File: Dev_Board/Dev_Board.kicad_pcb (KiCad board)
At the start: 2 copper layers, 13 parts

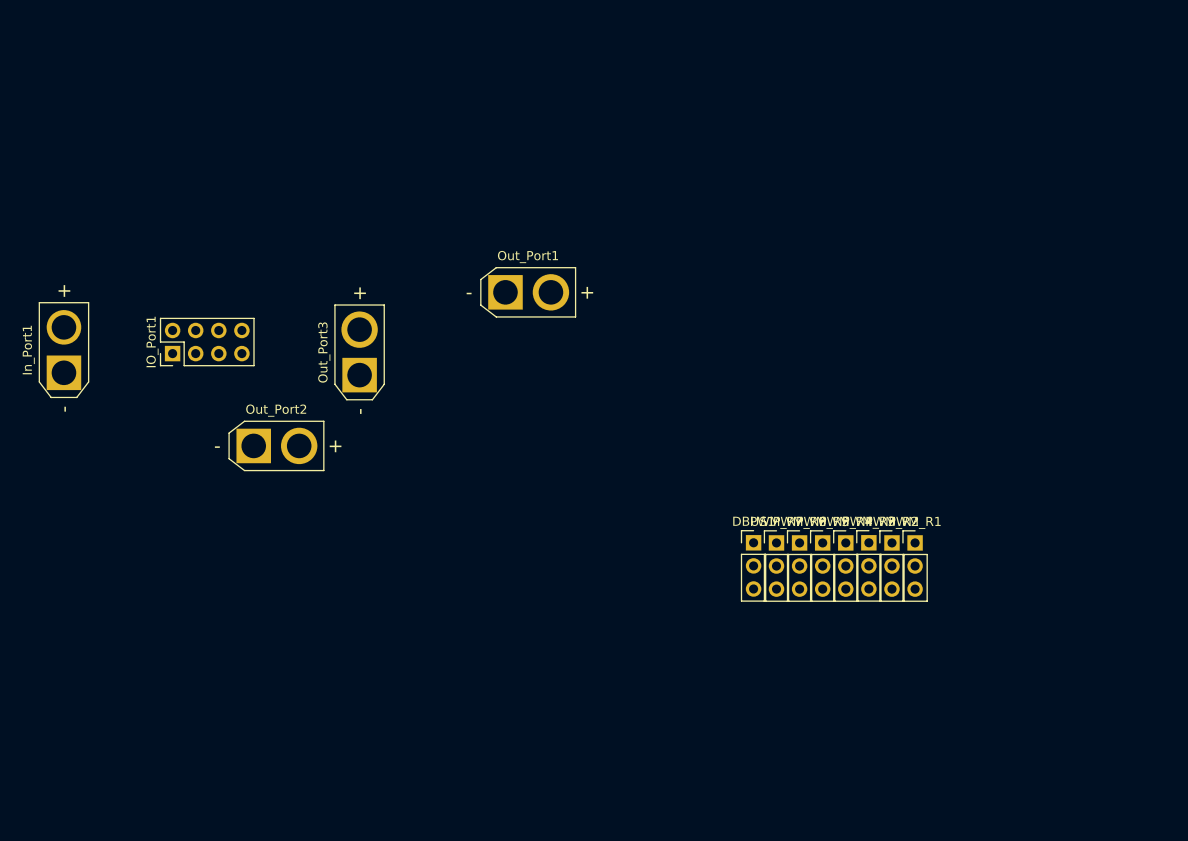
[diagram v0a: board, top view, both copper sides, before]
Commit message: added more pins to have different sets on the front and back sides. also changed the courtyards on some footprints because of errors. there are still like 3 courtyard errors
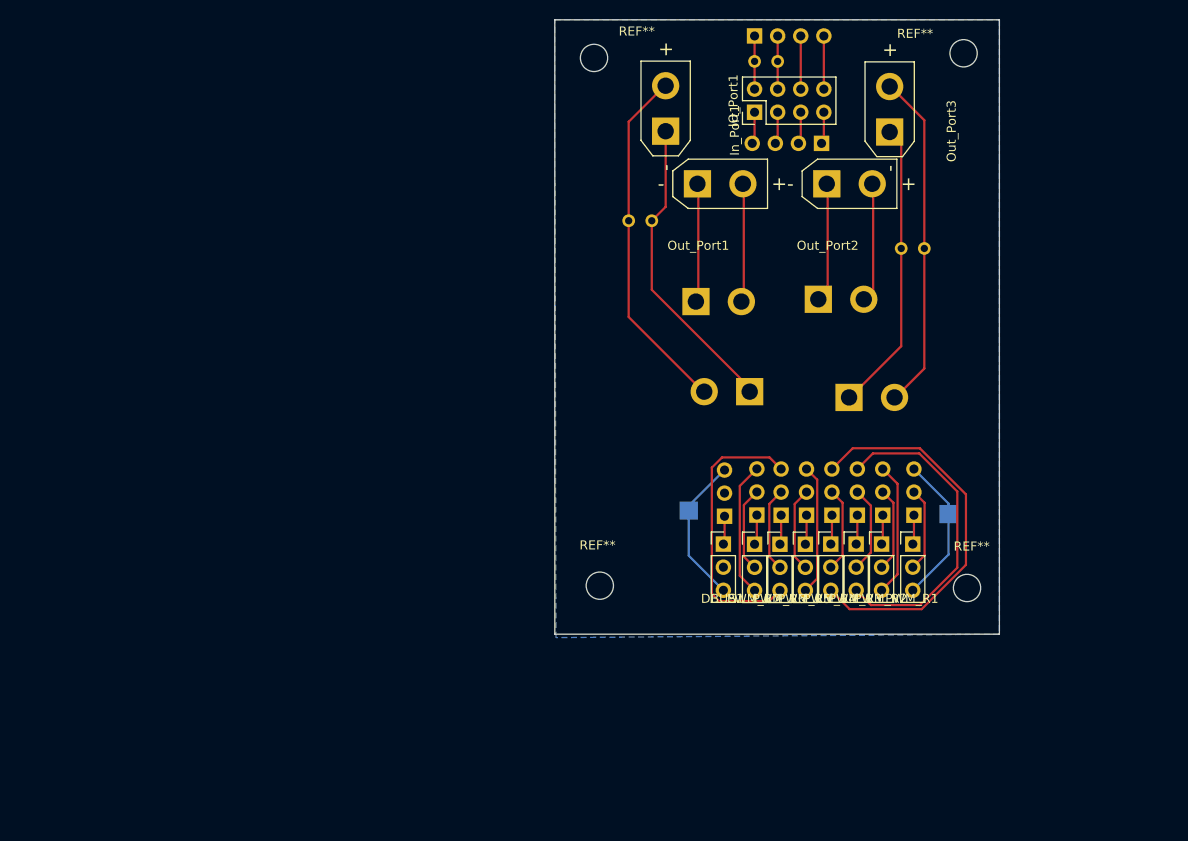
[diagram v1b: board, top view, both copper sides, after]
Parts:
- added DBUS2: Conn_01x03, dev_board_footprints:PinHeader_1x03_2.54mm_Vertical_small_courtyards, B.Cu at (196.8, 84.6)
- added In_Port2: Conn_01x02, dev_board_footprints:AMASS_XT30UPB-M_1x02_P5.0mm_Vertical_small_courtyards, B.Cu at (199.5, 70.9)
- added J1: Conn_01x04, Connector_PinHeader_2.54mm:PinHeader_1x04_P2.54mm_Vertical, B.Cu at (207.5, 43.6)
- added J2: Conn_01x04, Connector_PinHeader_2.54mm:PinHeader_1x04_P2.54mm_Vertical, B.Cu at (200.2, 31.8)
- added Out_Port4: Conn_01x02, dev_board_footprints:AMASS_XT30UPB-F_1x02_P5.0mm_Vertical_small_courtyards, B.Cu at (193.8, 61.0)
- added Out_Port5: Conn_01x02, dev_board_footprints:AMASS_XT30UPB-F_1x02_P5.0mm_Vertical_small_courtyards, B.Cu at (207.3, 60.7)
- added Out_Port6: Conn_01x02, dev_board_footprints:AMASS_XT30UPB-F_1x02_P5.0mm_Vertical_small_courtyards, B.Cu at (210.6, 71.5)
- added PWM_R10: Conn_01x03, dev_board_footprints:PinHeader_1x03_2.54mm_Vertical_small_courtyards, B.Cu at (211.5, 84.5)
- added PWM_R11: Conn_01x03, dev_board_footprints:PinHeader_1x03_2.54mm_Vertical_small_courtyards, B.Cu at (208.7, 84.5)
- added PWM_R12: Conn_01x03, dev_board_footprints:PinHeader_1x03_2.54mm_Vertical_small_courtyards, B.Cu at (205.9, 84.5)
- added PWM_R13: Conn_01x03, dev_board_footprints:PinHeader_1x03_2.54mm_Vertical_small_courtyards, B.Cu at (203.1, 84.5)
- added PWM_R14: Conn_01x03, dev_board_footprints:PinHeader_1x03_2.54mm_Vertical_small_courtyards, B.Cu at (200.4, 84.4)
- added PWM_R8: Conn_01x03, dev_board_footprints:PinHeader_1x03_2.54mm_Vertical_small_courtyards, B.Cu at (217.7, 84.5)
- added PWM_R9: Conn_01x03, dev_board_footprints:PinHeader_1x03_2.54mm_Vertical_small_courtyards, B.Cu at (214.2, 84.5)
- added REF**: MountingHole_3mm, MountingHole:MountingHole_3mm, F.Cu at (223.1, 33.7)
- added REF**: MountingHole_3mm, MountingHole:MountingHole_3mm, F.Cu at (223.5, 92.5)
- added REF**: MountingHole_3mm, MountingHole:MountingHole_3mm, F.Cu at (183.1, 92.2)
- added REF**: MountingHole_3mm, MountingHole:MountingHole_3mm, F.Cu at (182.5, 34.2)
- added TP1: TestPoint_2Pole, TestPoint:TestPoint_2Pads_Pitch2.54mm_Drill0.8mm, B.Cu at (200.2, 34.5)
- added TP2: TestPoint, TestPoint:TestPoint_Pad_2.0x2.0mm, B.Cu at (221.5, 84.3)
- added TP3: TestPoint, TestPoint:TestPoint_Pad_2.0x2.0mm, B.Cu at (192.9, 83.9)
- added TP4: TestPoint_2Pole, TestPoint:TestPoint_2Pads_Pitch2.54mm_Drill0.8mm, B.Cu at (188.8, 52.1)
- added TP5: TestPoint_2Pole, TestPoint:TestPoint_2Pads_Pitch2.54mm_Drill0.8mm, B.Cu at (216.3, 55.1)
- DBUS1, PWM_R1, PWM_R2, PWM_R3, PWM_R4, PWM_R5, PWM_R6, PWM_R7: footprint Connector_PinHeader_2.54mm:PinHeader_1x03_P2.54mm_Vertical -> dev_board_footprints:PinHeader_1x03_2.54mm_Vertical_small_courtyards
- In_Port1: footprint Connector_AMASS:AMASS_XT30U-M_1x02_P5.0mm_Vertical -> dev_board_footprints:AMASS_XT30UPB-M_1x02_P5.0mm_Vertical_small_courtyards
- Out_Port1, Out_Port2, Out_Port3: footprint Connector_AMASS:AMASS_XT30U-F_1x02_P5.0mm_Vertical -> dev_board_footprints:AMASS_XT30UPB-F_1x02_P5.0mm_Vertical_small_courtyards
- moved In_Port1 71.3 mm to (190.4, 42.1)
- moved Out_Port2 69.4 mm to (208.2, 48.0)
- moved IO_Port1 69.3 mm to (200.2, 40.1)
- moved Out_Port3 64.2 mm to (215.0, 42.2)
- moved Out_Port1 24.3 mm to (194.0, 48.0)
- moved DBUS1 3.33 mm to (196.7, 87.6)
- moved PWM_R7 2.42 mm to (200.2, 87.6)
- moved PWM_R6 2.16 mm to (202.9, 87.6)
- moved PWM_R5 1.91 mm to (205.7, 87.6)
- moved PWM_R4 1.66 mm to (208.5, 87.6)
- moved PWM_R3 1.40 mm to (211.3, 87.6)
- moved PWM_R2 1.15 mm to (214.1, 87.6)
- moved PWM_R1 0.28 mm to (217.6, 87.6)
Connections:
- In_Port1 pad 1: unconnected-(In_Port1-Pin_1-Pad1) -> Net-(In_Port1-Pin_1)
- In_Port1 pad 2: unconnected-(In_Port1-Pin_2-Pad2) -> Net-(In_Port1-Pin_2)
- Out_Port1 pad 1: unconnected-(Out_Port1-Pin_1-Pad1) -> Net-(Out_Port1-Pin_1)
- Out_Port1 pad 2: unconnected-(Out_Port1-Pin_2-Pad2) -> Net-(Out_Port1-Pin_2)
- Out_Port2 pad 1: unconnected-(Out_Port2-Pin_1-Pad1) -> Net-(Out_Port2-Pin_1)
- Out_Port2 pad 2: unconnected-(Out_Port2-Pin_2-Pad2) -> Net-(Out_Port2-Pin_2)
- Out_Port3 pad 1: unconnected-(Out_Port3-Pin_1-Pad1) -> Net-(Out_Port3-Pin_1)
- Out_Port3 pad 2: unconnected-(Out_Port3-Pin_2-Pad2) -> Net-(Out_Port3-Pin_2)
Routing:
- net /C4: track 0.00 -> 43.3 mm
- net Net-(In_Port1-Pin_2): track 0.00 -> 38.8 mm
- net Net-(Out_Port3-Pin_2): track 0.00 -> 37.2 mm
- net /C3: track 0.00 -> 35.3 mm
- net Net-(In_Port1-Pin_1): track 0.00 -> 35.0 mm
- net Net-(Out_Port3-Pin_1): track 0.00 -> 32.2 mm
- net /C6: track 0.00 -> 30.8 mm
- net /C1: track 0.00 -> 16.5 mm
- net /C8: track 0.00 -> 16.4 mm
- net /C7: track 0.00 -> 14.8 mm
- net /C2: track 0.00 -> 14.7 mm
- net /C5: track 0.00 -> 14.4 mm
- net Net-(Out_Port1-Pin_2): track 0.00 -> 13.5 mm
- net Net-(Out_Port1-Pin_1): track 0.00 -> 13.5 mm
- net Net-(Out_Port2-Pin_1): track 0.00 -> 13.2 mm
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- added copper zone on B.Cu, net /GND
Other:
- board outline added: 48.9 x 67.6 mm

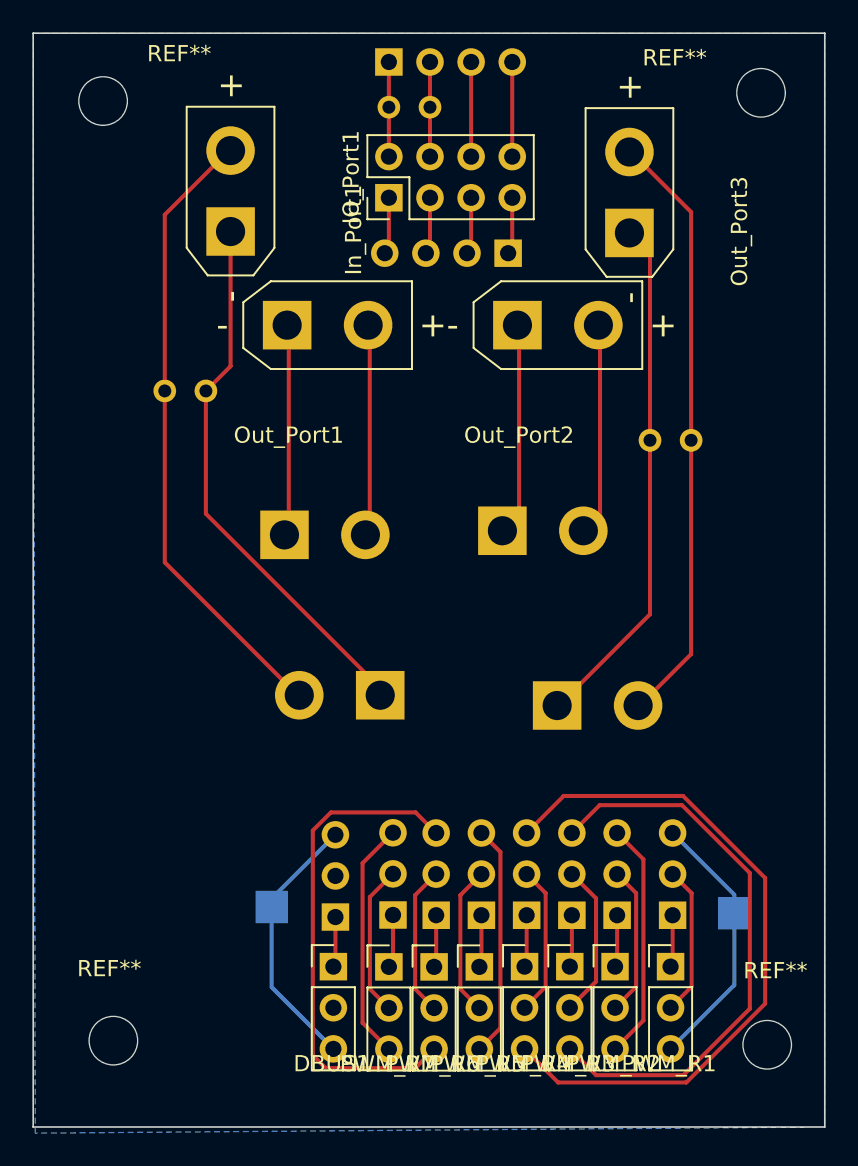
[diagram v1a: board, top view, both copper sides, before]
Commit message: fixed male parts, made tracks wider, made lakshay changes
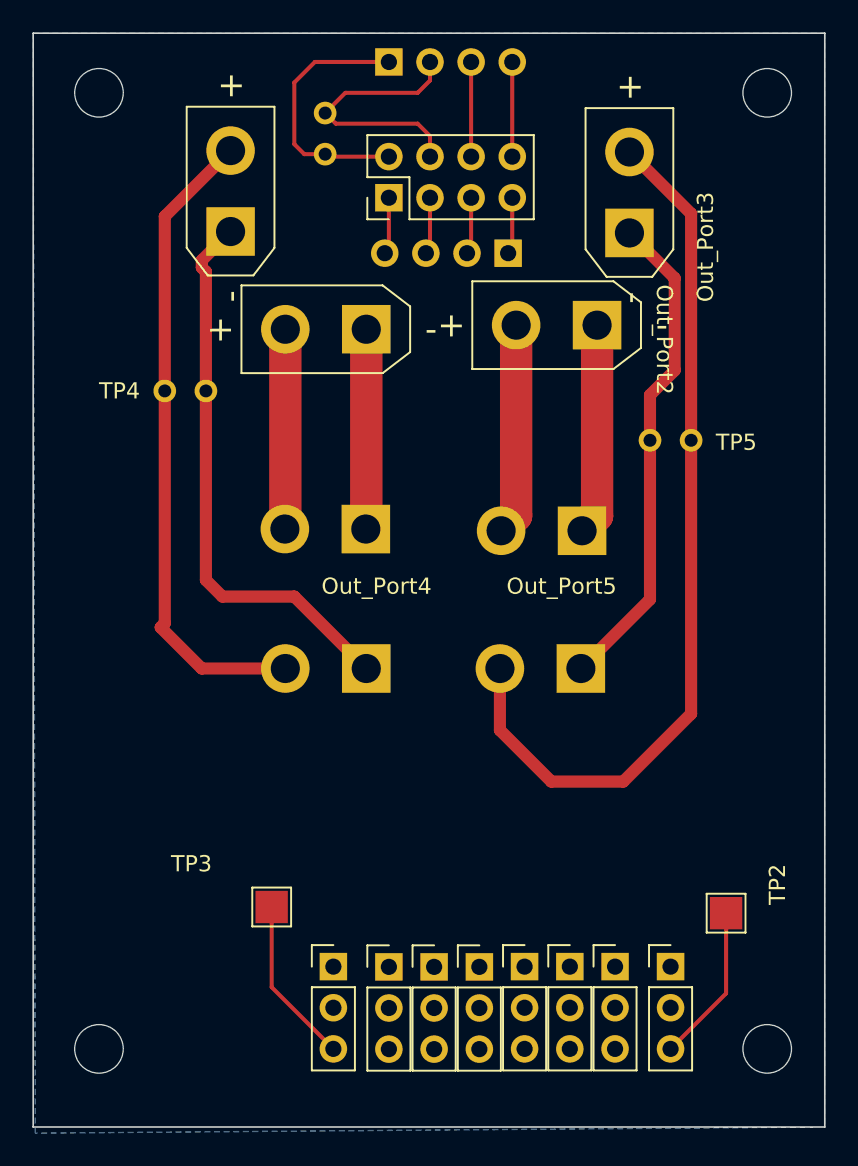
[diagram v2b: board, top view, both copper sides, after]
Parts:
- removed DBUS2, PWM_R10, PWM_R11, PWM_R12, PWM_R13, PWM_R14, PWM_R8, PWM_R9: Conn_01x03, dev_board_footprints:PinHeader_1x03_2.54mm_Vertical_small_courtyards
- removed REF** (x4): MountingHole_3mm, MountingHole:MountingHole_3mm
- added ?: , , F.Cu at (223.5, 92.7)
- added ?: , , F.Cu at (182.2, 92.7)
- added ?: , , F.Cu at (182.2, 33.7)
- added ?: , , F.Cu at (223.5, 33.7)
- TP2, TP3: moved to F.Cu
- moved TP1 4.89 mm to (196.2, 37.4), turned to 90 degrees
- moved Out_Port4 4.84 mm to (198.6, 60.6), turned to 180 degrees
- moved Out_Port2 4.72 mm to (212.9, 48.0), turned to 180 degrees
- moved Out_Port5 4.72 mm to (212.0, 60.7), turned to 180 degrees
- moved Out_Port1 4.69 mm to (198.7, 48.3), turned to 180 degrees
- moved Out_Port6 2.61 mm to (211.9, 69.2), turned to 180 degrees
- moved In_Port2 1.86 mm to (198.7, 69.2)
- moved TP2 0.51 mm to (221.0, 84.3), turned to 0 degrees
- turned TP3 to 0 degrees
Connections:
- net /3.3V renamed +3.3V
- DBUS1 pad 1: /A8 -> /A8M (GND)
- DBUS1 pad 2: /B8 -> /B8 (5V)
- IO_Port1 pad 2: /GND -> GND
- In_Port1 pad 1: Net-(In_Port1-Pin_1) -> GND
- In_Port1 pad 2: Net-(In_Port1-Pin_2) -> +24V
- In_Port2 pad 1: Net-(In_Port1-Pin_1) -> GND
- In_Port2 pad 2: Net-(In_Port1-Pin_2) -> +24V
- J2 pad 1: /GND -> GND
- Out_Port1 pad 1: Net-(Out_Port1-Pin_1) -> GND
- Out_Port1 pad 2: Net-(Out_Port1-Pin_2) -> +24V
- Out_Port2 pad 1: Net-(Out_Port2-Pin_1) -> GND
- Out_Port2 pad 2: Net-(Out_Port2-Pin_2) -> +24V
- Out_Port3 pad 1: Net-(Out_Port3-Pin_1) -> GND
- Out_Port3 pad 2: Net-(Out_Port3-Pin_2) -> +24V
- Out_Port4 pad 1: Net-(Out_Port1-Pin_1) -> GND
- Out_Port4 pad 2: Net-(Out_Port1-Pin_2) -> +24V
- Out_Port5 pad 1: Net-(Out_Port2-Pin_1) -> GND
- Out_Port5 pad 2: Net-(Out_Port2-Pin_2) -> +24V
- Out_Port6 pad 1: Net-(Out_Port3-Pin_1) -> GND
- Out_Port6 pad 2: Net-(Out_Port3-Pin_2) -> +24V
- PWM_R1 pad 1: /A1 -> /A1 (GND)
- PWM_R1 pad 2: /B1 -> /B1 (5V)
- TP1 pad 1: /GND -> GND
- TP4 pad 1: Net-(In_Port1-Pin_1) -> GND
- TP4 pad 2: Net-(In_Port1-Pin_2) -> +24V
- TP5 pad 1: Net-(Out_Port3-Pin_1) -> GND
- TP5 pad 2: Net-(Out_Port3-Pin_2) -> +24V
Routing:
- net +24V: track 0.00 -> 120.4 mm
- net GND: track 0.00 -> 108.3 mm
- net /C4: track 43.3 -> 0.00 mm
- net Net-(In_Port1-Pin_2): track 38.8 -> 0.00 mm
- net Net-(Out_Port3-Pin_2): track 37.2 -> 0.00 mm
- net /C3: track 35.3 -> 0.00 mm
- net Net-(In_Port1-Pin_1): track 35.0 -> 0.00 mm
- net Net-(Out_Port3-Pin_1): track 32.2 -> 0.00 mm
- net /C6: track 30.8 -> 0.00 mm
- net /C7: track 14.8 -> 0.00 mm
- net /C2: track 14.7 -> 0.00 mm
- net /C5: track 14.4 -> 0.00 mm
- net Net-(Out_Port1-Pin_2): track 13.5 -> 0.00 mm
- net Net-(Out_Port1-Pin_1): track 13.5 -> 0.00 mm
- net Net-(Out_Port2-Pin_1): track 13.2 -> 0.00 mm
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- added copper zone on B.Cu, net GND
- removed copper zone on B.Cu, net /GND

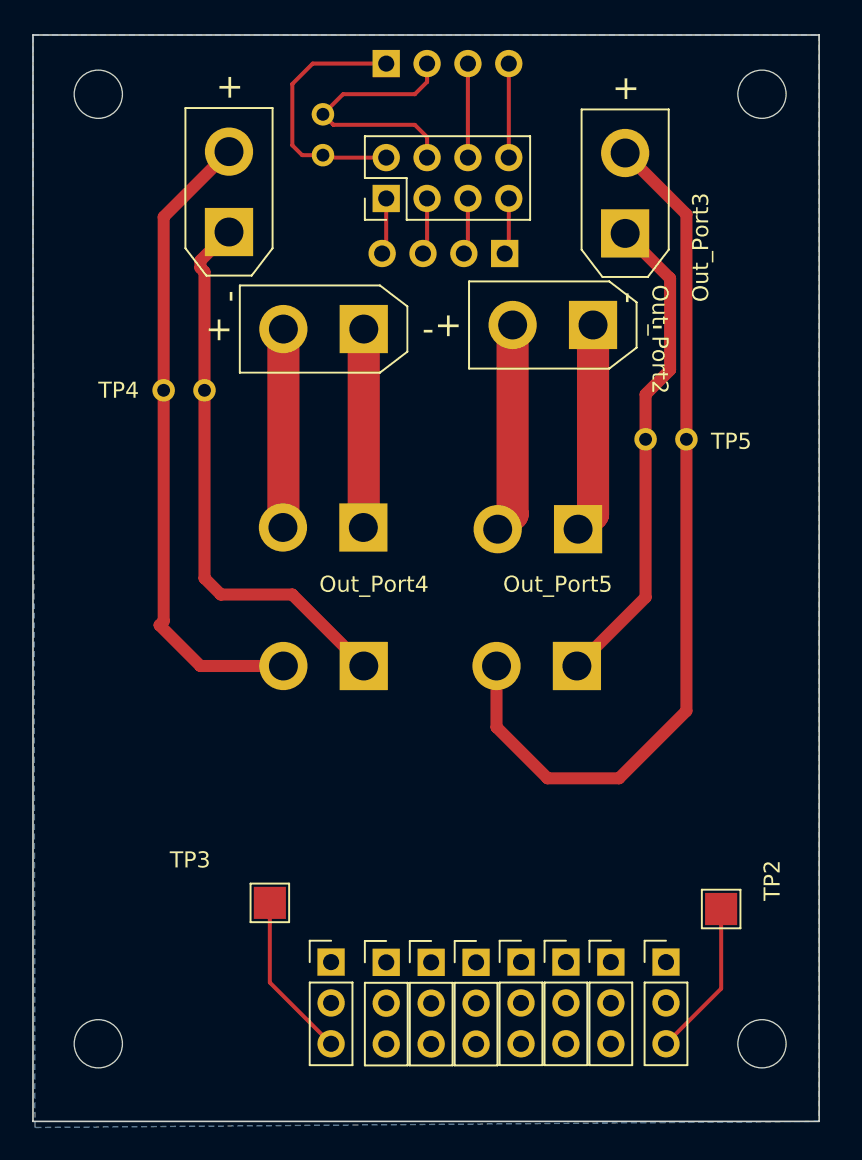
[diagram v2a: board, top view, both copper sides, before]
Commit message: didn't really make any changes b/c of meetings but the board might be too long and I will add connectors to the diodes next time
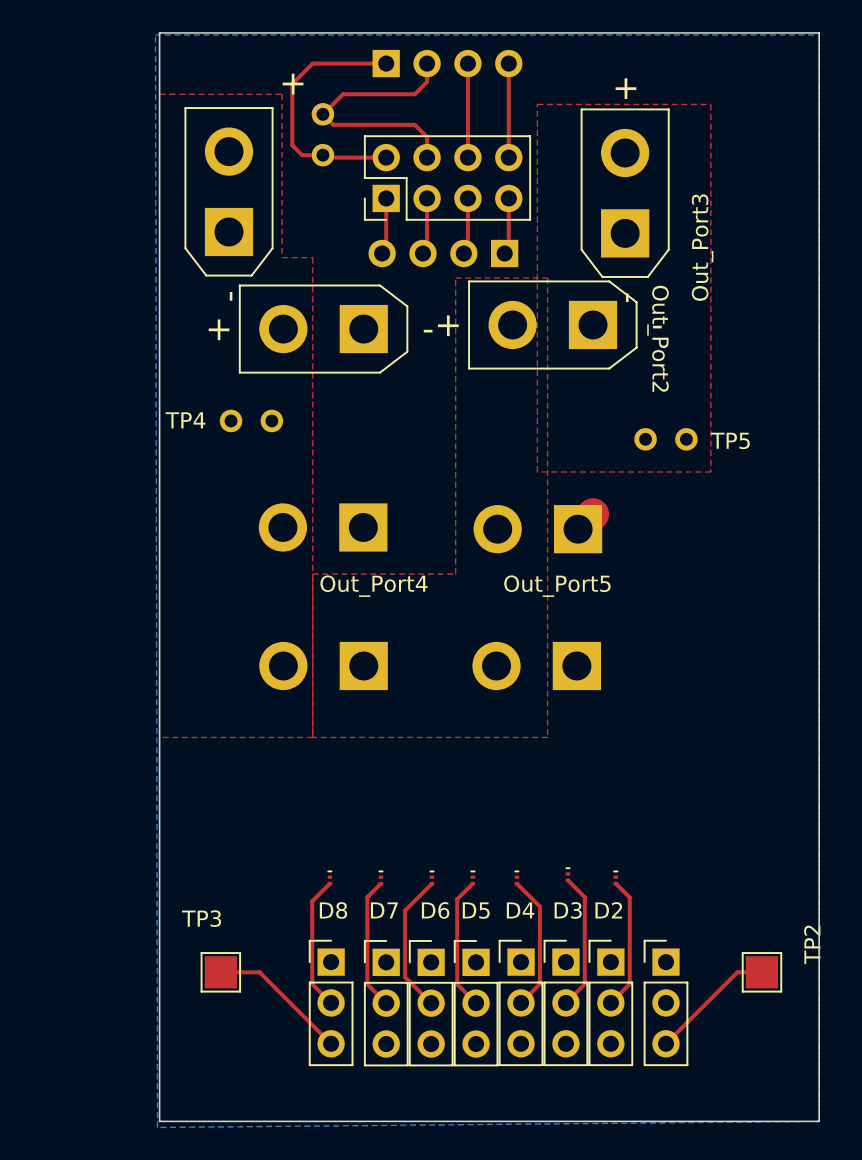
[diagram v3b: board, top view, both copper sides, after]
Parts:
- removed ? (x4): , 
- added D2: D, Diode_SMD:Nexperia_DSN0603-2_0.6x0.3mm_P0.4mm, F.Cu at (214.4, 82.5)
- added D3: D, Diode_SMD:Nexperia_DSN0603-2_0.6x0.3mm_P0.4mm, F.Cu at (211.5, 82.3)
- added D4: D, Diode_SMD:Nexperia_DSN0603-2_0.6x0.3mm_P0.4mm, F.Cu at (208.3, 82.5)
- added D5: D, Diode_SMD:Nexperia_DSN0603-2_0.6x0.3mm_P0.4mm, F.Cu at (205.5, 82.5)
- added D6: D, Diode_SMD:Nexperia_DSN0603-2_0.6x0.3mm_P0.4mm, F.Cu at (203.0, 82.5)
- added D7: D, Diode_SMD:Nexperia_DSN0603-2_0.6x0.3mm_P0.4mm, F.Cu at (199.8, 82.5)
- added D8: D, Diode_SMD:Nexperia_DSN0603-2_0.6x0.3mm_P0.4mm, F.Cu at (196.7, 82.5)
- moved TP3 5.29 mm to (189.9, 88.3)
- moved TP2 4.69 mm to (223.5, 88.3)
- moved TP4 4.60 mm to (193.0, 54.0)
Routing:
- net +24V: track 120.4 -> 0.14 mm
- net GND: track 108.3 -> 19.2 mm
- net /B6: track 0.00 -> 8.80 mm
- net /B3: track 0.00 -> 8.54 mm
- net /B4: track 0.00 -> 8.50 mm
- net /B8 (5V): track 0.00 -> 8.36 mm
- net /B5: track 0.00 -> 8.33 mm
- net /B7: track 0.00 -> 8.27 mm
- net /B2: track 0.00 -> 8.27 mm
- net /C1: track 9.80 -> 7.81 mm
- net /C8: track 10.3 -> 8.70 mm
- added copper zone on F.Cu, net +24V
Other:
- board size 48.9 x 67.6 mm -> 41 x 67.7 mm
